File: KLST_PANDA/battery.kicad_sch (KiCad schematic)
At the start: 19 parts, among them Q1 AO3401A, Q2 BCM857BS, SW3 SW_SPST, U4 TP5400

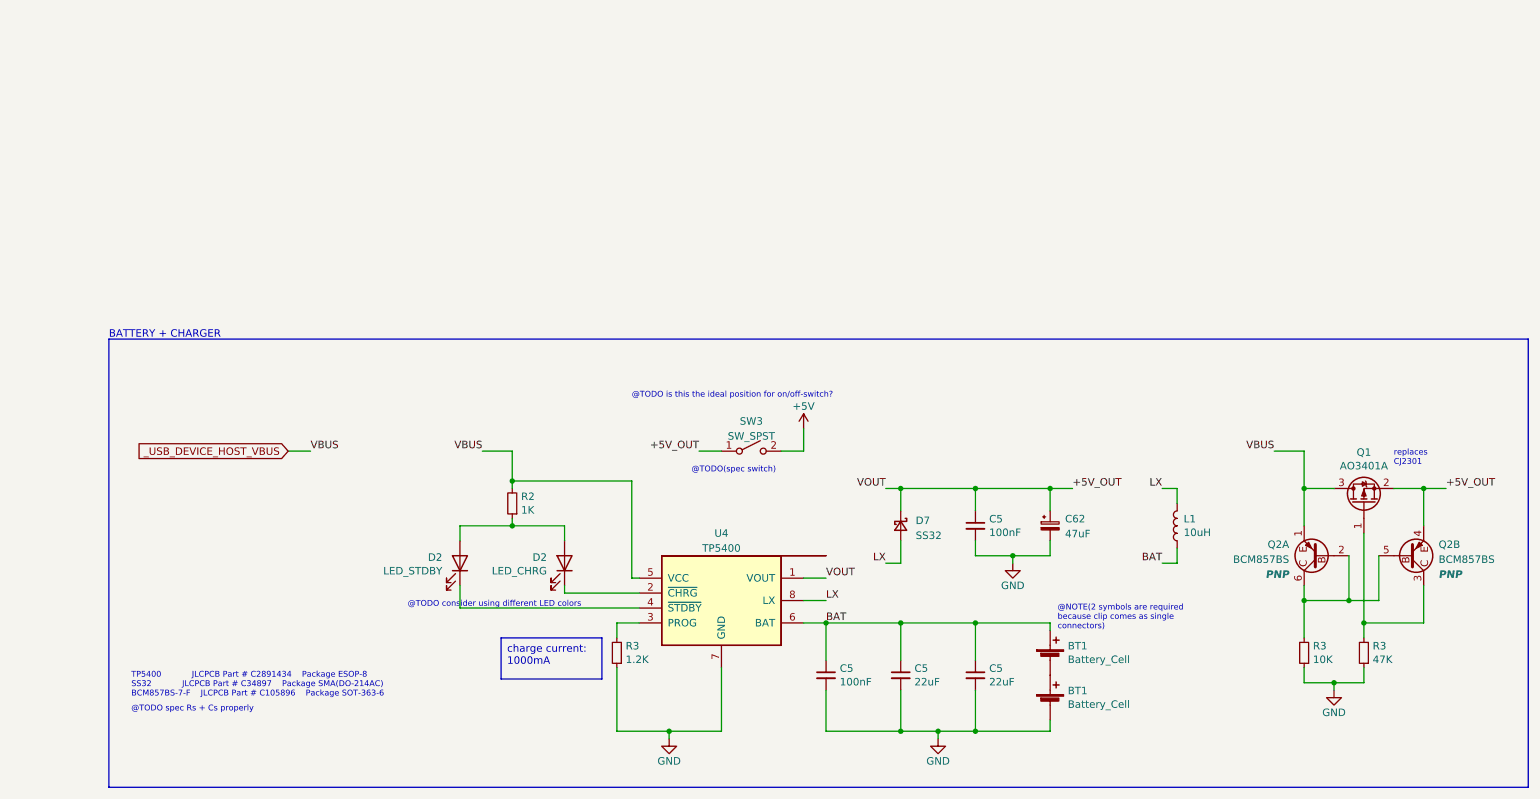
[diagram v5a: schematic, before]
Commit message: moved core (MCU) to sheet, cleaned up sheets
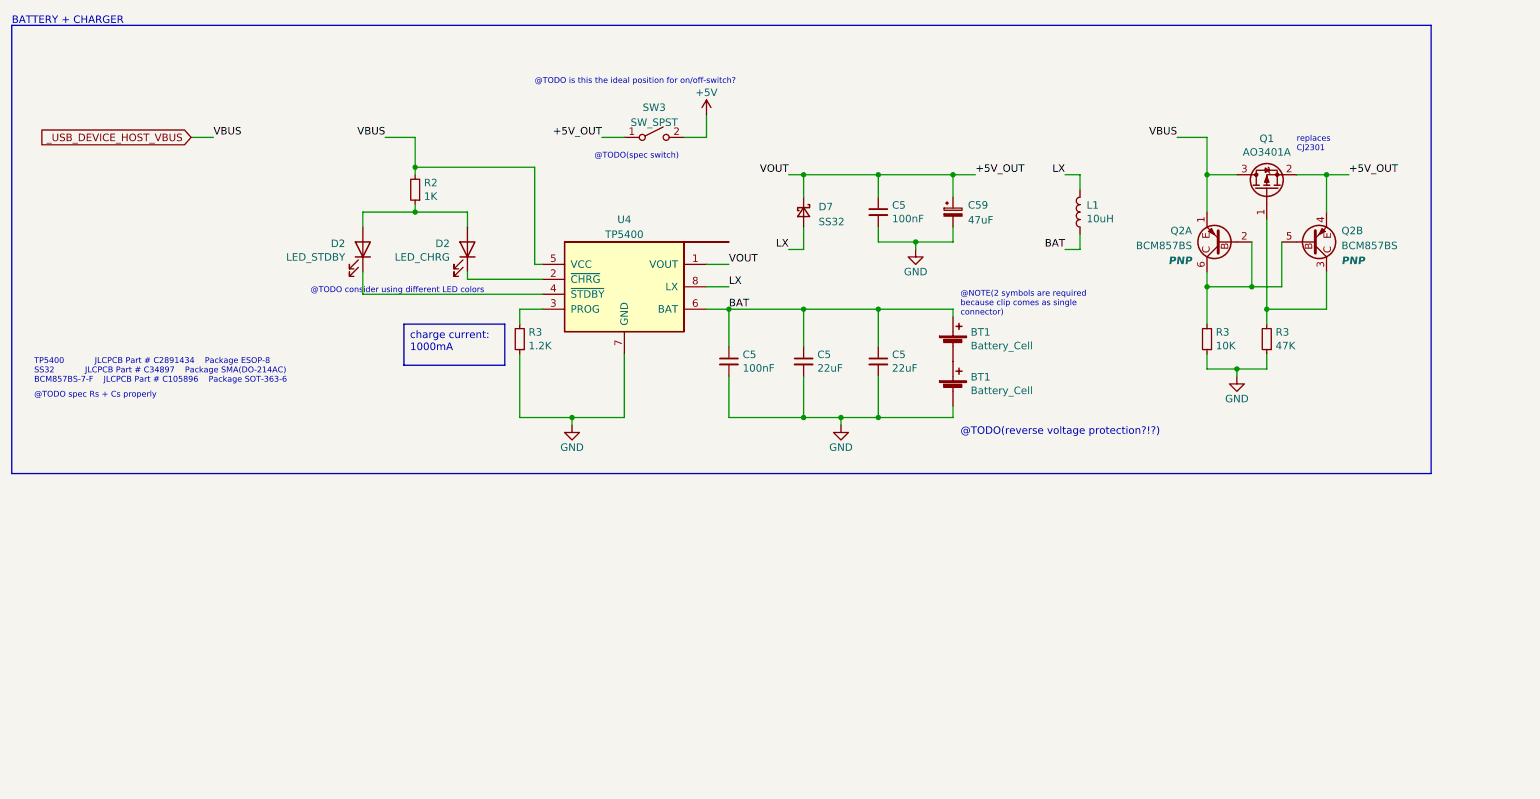
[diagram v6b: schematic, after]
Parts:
- renumbered C62 to C59
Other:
- note added: "@NOTE(2 symbols are required because clip comes as single connector)"
- note added: "@TODO(reverse voltage protection?!?)"
- note removed: "@NOTE(2 symbols are required because clip comes as single connectors)"
- moved on the sheet: BT1, C5, C59, D2, D7, L1, Q1, Q2A, Q2B, R2, R3, SW3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

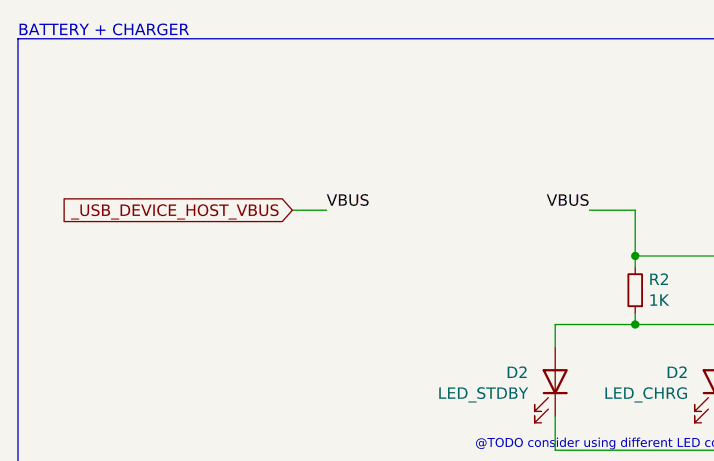
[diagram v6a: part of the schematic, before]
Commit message: started cleaning up schematic ( addressing DRC errors/warning ) (WIP)
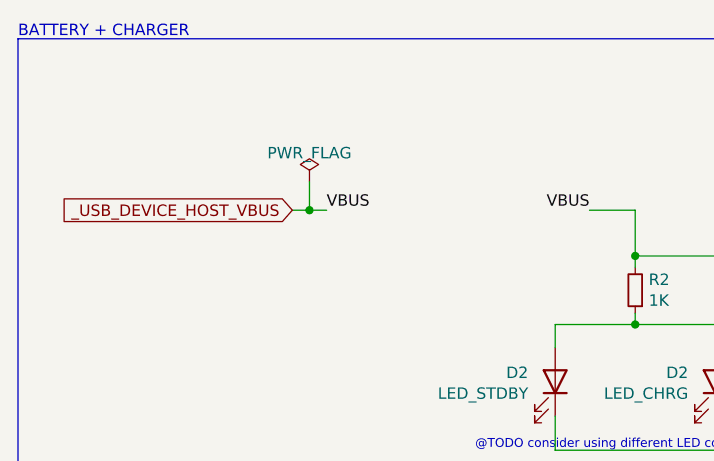
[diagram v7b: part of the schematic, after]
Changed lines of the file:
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@@
 (kicad_sch (version 20230121) (generator eeschema)
   (paper "A4")
+  (junction (at 47.625 34.29) (diameter 0) (color 0 0 0 0)
+  )
   (junction (at 218.44 40.64) (diameter 0) (color 0 0 0 0)
   )
@@
     (stroke (width 0) (type default))
   )
-  (wire (pts (xy 45.72 34.29) (xy 49.53 34.29))
+  (wire (pts (xy 45.72 34.29) (xy 47.625 34.29))
     (stroke (width 0) (type default))
   )
@@
     (stroke (width 0) (type default))
   )
+  (wire (pts (xy 47.625 31.115) (xy 47.625 34.29))
+    (stroke (width 0) (type default))
+  )
   (wire (pts (xy 162.56 74.93) (xy 162.56 81.915))
     (stroke (width 0) (type default))
@@
   )
   (wire (pts (xy 149.86 40.64) (xy 147.32 40.64))
+    (stroke (width 0) (type default))
+  )
+  (wire (pts (xy 47.625 34.29) (xy 49.53 34.29))
     (stroke (width 0) (type default))
   )
@@
       (project "KLST_PANDA"
         (path "/b4513875-4c57-4720-bcc5-43ead67fe18f/82e35567-f058-4d94-a9b9-5b3354666c47"
-          (reference "#PWR052") (unit 1)
+          (reference "#PWR053") (unit 1)
         )
       )
@@
       (project "KLST_PANDA"
         (path "/b4513875-4c57-4720-bcc5-43ead67fe18f/82e35567-f058-4d94-a9b9-5b3354666c47"
-          (reference "#PWR053") (unit 1)
+          (reference "#PWR054") (unit 1)
         )
       )
@@
       (project "KLST_PANDA"
         (path "/b4513875-4c57-4720-bcc5-43ead67fe18f/82e35567-f058-4d94-a9b9-5b3354666c47"
-          (reference "#PWR055") (unit 1)
+          (reference "#PWR056") (unit 1)
         )
       )
@@
       (project "KLST_PANDA"
         (path "/b4513875-4c57-4720-bcc5-43ead67fe18f/82e35567-f058-4d94-a9b9-5b3354666c47"
-          (reference "#PWR054") (unit 1)
+          (reference "#PWR055") (unit 1)
         )
       )
@@
       (project "KLST_PANDA"
         (path "/b4513875-4c57-4720-bcc5-43ead67fe18f/82e35567-f058-4d94-a9b9-5b3354666c47"
-          (reference "#PWR051") (unit 1)
-        )
-      )
+          (reference "#PWR052") (unit 1)
+        )
+      )
+    )
+  )
+  (symbol (lib_id "power:PWR_FLAG") (at 47.625 31.115 0) (unit 1)
+    (in_bom yes) (on_board yes) (dnp no) (fields_autoplaced)
+    (property "Reference" "#FLG08" (at 47.625 29.21 0)
+      (effects (font (size 1.27 1.27)) hide)
+    )
+    (property "Value" "PWR_FLAG" (at 47.625 27.94 0)
+      (effects (font (size 1.27 1.27)))
+    )
+    (property "Footprint" "" (at 47.625 31.115 0)
+      (effects (font (size 1.27 1.27)) hide)
+    )
+    (property "Datasheet" "~" (at 47.625 31.115 0)
+      (effects (font (size 1.27 1.27)) hide)
+    )
+    (pin "1")
+    (instances
+      (project "KLST_PANDA"
+        (path "/b4513875-4c57-4720-bcc5-43ead67fe18f/82e35567-f058-4d94-a9b9-5b3354666c47"
+          (reference "#FLG08") (unit 1)
+        )
+      )

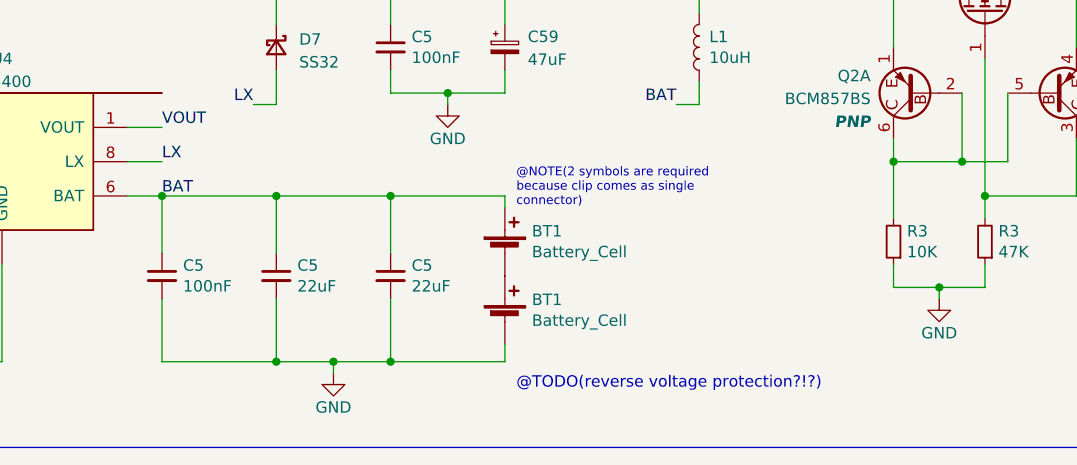
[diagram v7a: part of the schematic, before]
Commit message: added battery clip, updated to new KiCad version
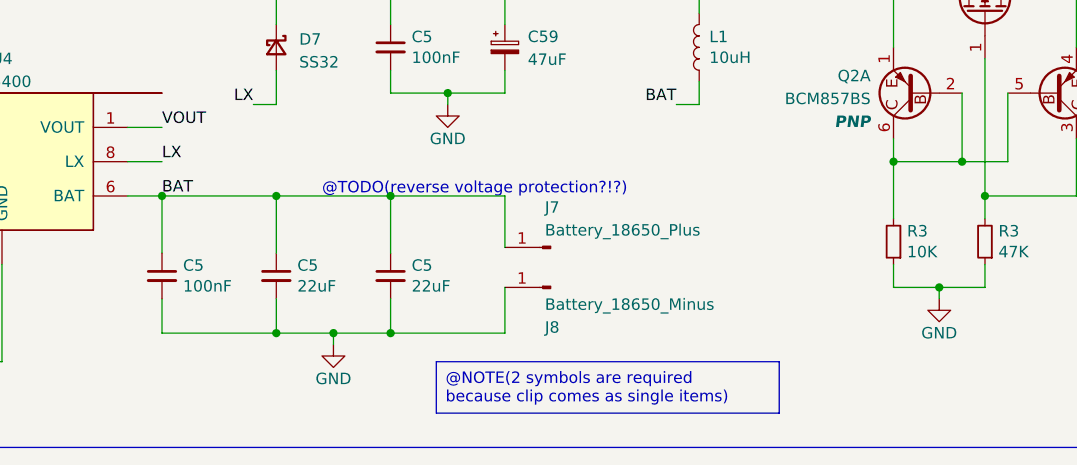
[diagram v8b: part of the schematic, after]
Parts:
- removed BT1 (x2): Battery_Cell, KLST_GRASS:Keystone Electronics - PC Battery Clip #54, symbol Device:Battery_Cell
- added J7: Battery_18650_Plus, MY-18650-01:MY-18650-01, symbol Connector:Conn_01x01_Pin
- added J8: Battery_18650_Minus, MY-18650-01:MY-18650-01, symbol Connector:Conn_01x01_Pin
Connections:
- net BAT: now also J7.1 (Pin_1)
- net GND: now also J8.1 (Pin_1)
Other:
- note removed: "@NOTE(2 symbols are required because clip comes as single connector)"
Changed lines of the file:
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@@
   (junction (at 223.52 73.66) (diameter 0) (color 0 0 0 0)
   )
-  (junction (at 156.21 81.915) (diameter 0) (color 0 0 0 0)
-  )
-  (junction (at 149.86 81.915) (diameter 0) (color 0 0 0 0)
+  (junction (at 156.21 78.74) (diameter 0) (color 0 0 0 0)
+  )
+  (junction (at 149.86 78.74) (diameter 0) (color 0 0 0 0)
   )
   (junction (at 162.56 40.64) (diameter 0) (color 0 0 0 0)
   )
+  (junction (at 162.56 78.74) (diameter 0) (color 0 0 0 0)
+  )
   (junction (at 175.26 40.64) (diameter 0) (color 0 0 0 0)
   )
@@
   (junction (at 83.82 46.99) (diameter 0) (color 0 0 0 0)
   )
-  (junction (at 162.56 81.915) (diameter 0) (color 0 0 0 0)
-  )
   (junction (at 168.91 52.07) (diameter 0) (color 0 0 0 0)
   )
@@
     (stroke (width 0) (type default))
   )
+  (wire (pts (xy 175.26 78.74) (xy 175.26 73.66))
+    (stroke (width 0) (type default))
+  )
   (wire (pts (xy 149.86 69.85) (xy 149.86 63.5))
     (stroke (width 0) (type default))
   )
-  (wire (pts (xy 137.16 81.915) (xy 149.86 81.915))
+  (wire (pts (xy 137.16 78.74) (xy 149.86 78.74))
     (stroke (width 0) (type default))
   )
@@
     (stroke (width 0) (type default))
   )
-  (wire (pts (xy 149.86 81.915) (xy 156.21 81.915))
+  (wire (pts (xy 149.86 78.74) (xy 156.21 78.74))
     (stroke (width 0) (type default))
   )
@@
     (stroke (width 0) (type default))
   )
-  (wire (pts (xy 175.26 80.01) (xy 175.26 81.915))
-    (stroke (width 0) (type default))
-  )
   (wire (pts (xy 168.91 52.07) (xy 175.26 52.07))
     (stroke (width 0) (type default))
@@
     (stroke (width 0) (type default))
   )
+  (wire (pts (xy 149.86 74.93) (xy 149.86 78.74))
+    (stroke (width 0) (type default))
+  )
   (wire (pts (xy 238.76 40.64) (xy 242.57 40.64))
     (stroke (width 0) (type default))
@@
     (stroke (width 0) (type default))
   )
-  (wire (pts (xy 137.16 74.93) (xy 137.16 81.915))
+  (wire (pts (xy 137.16 74.93) (xy 137.16 78.74))
     (stroke (width 0) (type default))
   )
@@
     (stroke (width 0) (type default))
   )
-  (wire (pts (xy 149.86 74.93) (xy 149.86 81.915))
-    (stroke (width 0) (type default))
-  )
   (wire (pts (xy 218.44 73.66) (xy 223.52 73.66))
     (stroke (width 0) (type default))
@@
     (stroke (width 0) (type default))
   )
-  (wire (pts (xy 156.21 81.915) (xy 162.56 81.915))
+  (wire (pts (xy 156.21 78.74) (xy 162.56 78.74))
     (stroke (width 0) (type default))
   )
@@
     (stroke (width 0) (type default))
   )
-  (wire (pts (xy 162.56 74.93) (xy 162.56 81.915))
-    (stroke (width 0) (type default))
-  )
-  (wire (pts (xy 156.21 81.915) (xy 156.21 83.185))
+  (wire (pts (xy 156.21 78.74) (xy 156.21 80.01))
     (stroke (width 0) (type default))
   )
@@
     (stroke (width 0) (type default))
   )
-  (wire (pts (xy 175.26 63.5) (xy 175.26 64.77))
+  (wire (pts (xy 175.26 63.5) (xy 175.26 69.215))
     (stroke (width 0) (type default))
   )
@@
     (stroke (width 0) (type default))
   )
+  (wire (pts (xy 162.56 74.93) (xy 162.56 78.74))
+    (stroke (width 0) (type default))
+  )
   (wire (pts (xy 115.57 34.29) (xy 119.38 34.29))
     (stroke (width 0) (type default))
@@
     (stroke (width 0) (type default))
   )
-  (wire (pts (xy 175.26 81.915) (xy 162.56 81.915))
+  (wire (pts (xy 175.26 78.74) (xy 162.56 78.74))
     (stroke (width 0) (type default))
   )
@@
     (stroke (width 0) (type default))
     (fill (type none))
+  )
+  (text_box "@NOTE(2 symbols are required because clip comes as single items)"
+    (at 167.64 81.915 0) (size 38.1 5.715)
+    (stroke (width 0) (type default))
+    (fill (type none))
+    (effects (font (size 1.27 1.27)) (justify left top))
   )
   (text_box "charge current:\n1000mA"
@@
     (fill (type none))
     (effects (font (size 1.27 1.27)) (justify left top))
-  )
-  (text "@NOTE(2 symbols are required \nbecause clip comes as single \nconnector)"
-    (at 176.53 64.77 0)
-    (effects (font (size 0.9906 0.9906)) (justify left bottom))
   )
   (text "TP5400			JLCPCB Part # C2891434	Package ESOP-8\nSS32			JLCPCB Part # C34897	Package SMA(DO-214AC)\nBCM857BS-7-F	JLCPCB Part # C105896	Package SOT-363-6\n"
@@
     (effects (font (size 0.9906 0.9906)) (justify left bottom))
   )
-  (text "@TODO(reverse voltage protection?!?)" (at 176.53 85.09 0)
+  (text "@TODO(reverse voltage protection?!?)" (at 154.94 63.5 0)
     (effects (font (size 1.27 1.27)) (justify left bottom))
   )
@@
     )
   )
-  (symbol (lib_id "Device:Battery_Cell") (at 175.26 69.85 0) (unit 1)
-    (in_bom yes) (on_board yes) (dnp no)
-    (property "Reference" "BT1" (at 178.2572 67.4116 0)
-      (effects (font (size 1.27 1.27)) (justify left))
-    )
-    (property "Value" "Battery_Cell" (at 178.2572 69.723 0)
-      (effects (font (size 1.27 1.27)) (justify left))
-    )
-    (property "Footprint" "KLST_GRASS:Keystone Electronics - PC Battery Clip #54" (at 175.26 68.326 90)
-      (effects (font (size 1.27 1.27)) hide)
-    )
-    (property "Datasheet" "~" (at 175.26 68.326 90)
-      (effects (font (size 1.27 1.27)) hide)
-    )
-    (property "JLCPCB Part #" "C2979183" (at 175.26 69.85 0)
-      (effects (font (size 1.27 1.27)) hide)
-    )
-    (pin "1")
-    (pin "2")
-    (instances
-      (project "KLST_GRASS"
-        (path "/19c93e10-6fa1-4cb5-a74e-4164e52256d7"
-          (reference "BT1") (unit 1)
-        )
-      )
-      (project "KLST_PANDA"
-        (path "/b4513875-4c57-4720-bcc5-43ead67fe18f/82e35567-f058-4d94-a9b9-5b3354666c47"
-          (reference "BT1") (unit 1)
-        )
-      )
-    )
-  )
-  (symbol (lib_id "power:GND") (at 156.21 83.185 0) (unit 1)
-    (in_bom yes) (on_board yes) (dnp no)
-    (property "Reference" "#PWR01" (at 156.21 89.535 0)
-      (effects (font (size 1.27 1.27)) hide)
-    )
-    (property "Value" "GND" (at 156.21 86.995 0)
+  (symbol (lib_id "power:GND") (at 156.21 80.01 0) (unit 1)
+    (in_bom yes) (on_board yes) (dnp no)
+    (property "Reference" "#PWR01" (at 156.21 86.36 0)
+      (effects (font (size 1.27 1.27)) hide)
+    )
+    (property "Value" "GND" (at 156.21 83.82 0)
       (effects (font (size 1.27 1.27)))
     )
-    (property "Footprint" "" (at 156.21 83.185 0)
-      (effects (font (size 1.27 1.27)) hide)
-    )
-    (property "Datasheet" "" (at 156.21 83.185 0)
+    (property "Footprint" "" (at 156.21 80.01 0)
+      (effects (font (size 1.27 1.27)) hide)
+    )
+    (property "Datasheet" "" (at 156.21 80.01 0)
       (effects (font (size 1.27 1.27)) hide)
     )
@@
     )
   )
-  (symbol (lib_id "Device:Battery_Cell") (at 175.26 77.47 0) (unit 1)
-    (in_bom yes) (on_board yes) (dnp no)
-    (property "Reference" "BT1" (at 178.2572 75.0316 0)
-      (effects (font (size 1.27 1.27)) (justify left))
-    )
-    (property "Value" "Battery_Cell" (at 178.2572 77.343 0)
-      (effects (font (size 1.27 1.27)) (justify left))
-    )
-    (property "Footprint" "KLST_GRASS:Keystone Electronics - PC Battery Clip #54" (at 175.26 75.946 90)
-      (effects (font (size 1.27 1.27)) hide)
-    )
-    (property "Datasheet" "~" (at 175.26 75.946 90)
-      (effects (font (size 1.27 1.27)) hide)
-    )
-    (property "JLCPCB Part #" "C2979183" (at 175.26 77.47 0)
-      (effects (font (size 1.27 1.27)) hide)
-    )
-    (pin "1")
-    (pin "2")
-    (instances
-      (project "KLST_GRASS"
-        (path "/19c93e10-6fa1-4cb5-a74e-4164e52256d7"
-          (reference "BT1") (unit 1)
-        )
-      )
-      (project "KLST_PANDA"
-        (path "/b4513875-4c57-4720-bcc5-43ead67fe18f/82e35567-f058-4d94-a9b9-5b3354666c47"
-          (reference "BT2") (unit 1)
+  (symbol (lib_id "Connector:Conn_01x01_Pin") (at 180.34 73.66 0) (mirror y) (unit 1)
+    (in_bom yes) (on_board yes) (dnp no)
+    (property "Reference" "J8" (at 179.705 78.105 0)
+      (effects (font (size 1.27 1.27)) (justify right))
+    )
+    (property "Value" "Battery_18650_Minus" (at 179.705 75.565 0)
+      (effects (font (size 1.27 1.27)) (justify right))
+    )
+    (property "Footprint" "MY-18650-01:MY-18650-01" (at 180.34 73.66 0)
+      (effects (font (size 1.27 1.27)) hide)
+    )
+    (property "Datasheet" "~" (at 180.34 73.66 0)
+      (effects (font (size 1.27 1.27)) hide)
+    )
+    (pin "1")
+    (instances
+      (project "KLST_PANDA"
+        (path "/b4513875-4c57-4720-bcc5-43ead67fe18f/82e35567-f058-4d94-a9b9-5b3354666c47"
+          (reference "J8") (unit 1)
         )
       )
@@
         )
       )
+    )
+  )
+  (symbol (lib_id "Connector:Conn_01x01_Pin") (at 180.34 69.215 180) (unit 1)
+    (in_bom yes) (on_board yes) (dnp no)
+    (property "Reference" "J7" (at 179.705 64.77 0)
+      (effects (font (size 1.27 1.27)) (justify right))
+    )
+    (property "Value" "Battery_18650_Plus" (at 179.705 67.31 0)
+      (effects (font (size 1.27 1.27)) (justify right))
+    )
+    (property "Footprint" "MY-18650-01:MY-18650-01" (at 180.34 69.215 0)
+      (effects (font (size 1.27 1.27)) hide)
+    )
+    (property "Datasheet" "~" (at 180.34 69.215 0)
+      (effects (font (size 1.27 1.27)) hide)
+    )
+    (pin "1")
+    (instances
+      (project "KLST_PANDA"
+        (path "/b4513875-4c57-4720-bcc5-43ead67fe18f/82e35567-f058-4d94-a9b9-5b3354666c47"
+          (reference "J7") (unit 1)
+        )
+      )
